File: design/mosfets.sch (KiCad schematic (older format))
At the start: 15 parts, among them Q1 Si2302CDS, Q2 Si2302CDS, Q3 Si2302CDS, Q4 Si2302CDS, Q5 Si2302CDS, Q6 Si2302CDS

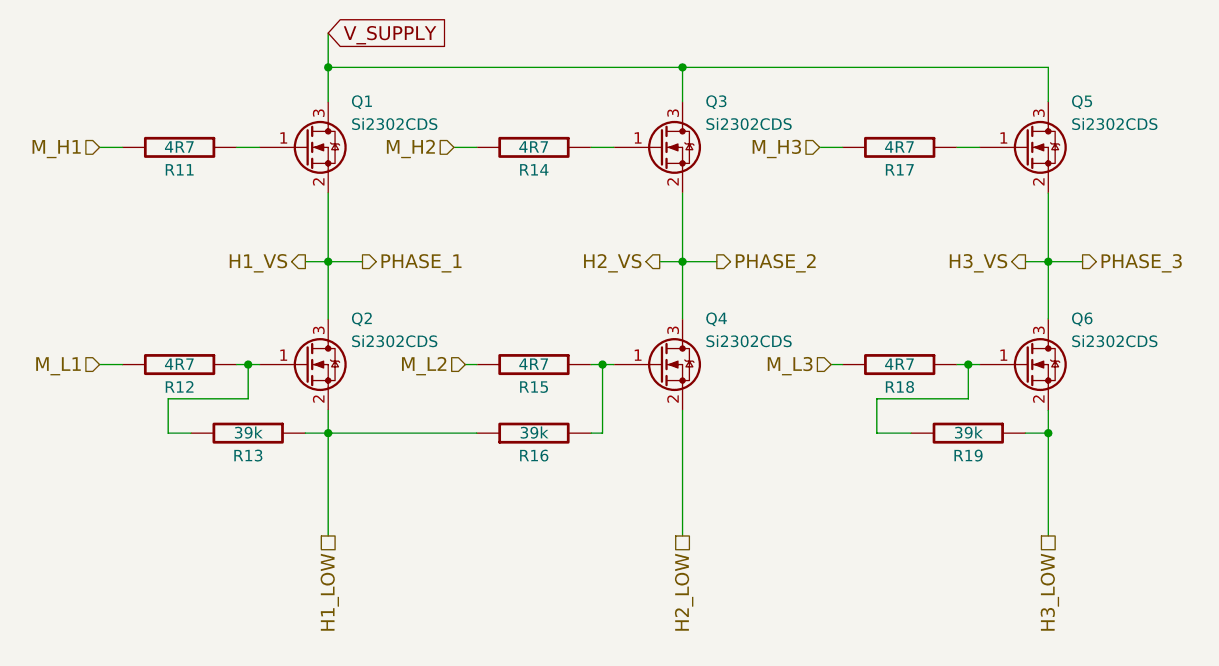
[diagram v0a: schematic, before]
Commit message: Added BOM and reworked component naming to be inline with old VESC names
:^)
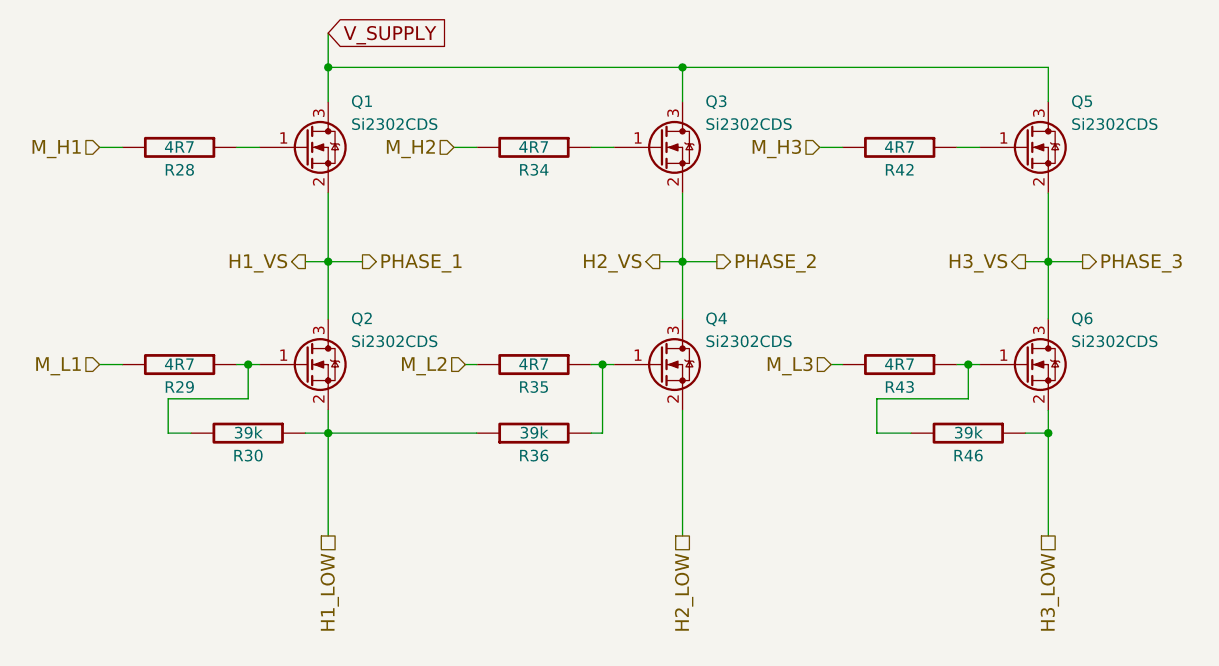
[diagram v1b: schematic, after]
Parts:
- renumbered R11 to R28, R12 to R29, R13 to R30, R14 to R34, R15 to R35, R16 to R36, R17 to R42, R18 to R43, R19 to R46
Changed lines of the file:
@@
 $EndDescr
 $Comp
-L BLDC_4-rescue:R-RESCUE-BLDC_4 R19
+L BLDC_4-rescue:R-RESCUE-BLDC_4 R46
 U 1 1 53F8E60B
 P 7850 4050
-F 0 "R19" V 7950 4050 50  0000 C CNN
+F 0 "R46" V 7950 4050 50  0000 C CNN
 F 1 "39k" V 7850 4050 50  0000 C CNN
 F 2 "Resistor_SMD:R_0603_1608Metric" H 7850 4050 60  0001 C CNN
@@
 $EndComp
 $Comp
-L BLDC_4-rescue:R-RESCUE-BLDC_4 R13
+L BLDC_4-rescue:R-RESCUE-BLDC_4 R30
 U 1 1 53F8E612
 P 4700 4050
-F 0 "R13" V 4800 4050 50  0000 C CNN
+F 0 "R30" V 4800 4050 50  0000 C CNN
 F 1 "39k" V 4700 4050 50  0000 C CNN
 F 2 "Resistor_SMD:R_0603_1608Metric" H 4700 4050 60  0001 C CNN
@@
 $EndComp
 $Comp
-L BLDC_4-rescue:R-RESCUE-BLDC_4 R12
+L BLDC_4-rescue:R-RESCUE-BLDC_4 R29
 U 1 1 53F8E64B
 P 4400 3750
-F 0 "R12" V 4500 3750 50  0000 C CNN
+F 0 "R29" V 4500 3750 50  0000 C CNN
 F 1 "4R7" V 4400 3750 50  0000 C CNN
 F 2 "Resistor_SMD:R_0603_1608Metric" H 4400 3750 60  0001 C CNN
@@
 $EndComp
 $Comp
-L BLDC_4-rescue:R-RESCUE-BLDC_4 R11
+L BLDC_4-rescue:R-RESCUE-BLDC_4 R28
 U 1 1 53F8E652
 P 4400 2800
-F 0 "R11" V 4500 2800 50  0000 C CNN
+F 0 "R28" V 4500 2800 50  0000 C CNN
 F 1 "4R7" V 4400 2800 50  0000 C CNN
 F 2 "Resistor_SMD:R_0603_1608Metric" H 4400 2800 60  0001 C CNN
@@
 $EndComp
 $Comp
-L BLDC_4-rescue:R-RESCUE-BLDC_4 R14
+L BLDC_4-rescue:R-RESCUE-BLDC_4 R34
 U 1 1 53F8E65E
 P 5950 2800
-F 0 "R14" V 6050 2800 50  0000 C CNN
+F 0 "R34" V 6050 2800 50  0000 C CNN
 F 1 "4R7" V 5950 2800 50  0000 C CNN
 F 2 "Resistor_SMD:R_0603_1608Metric" H 5950 2800 60  0001 C CNN
@@
 $EndComp
 $Comp
-L BLDC_4-rescue:R-RESCUE-BLDC_4 R15
+L BLDC_4-rescue:R-RESCUE-BLDC_4 R35
 U 1 1 53F8E665
 P 5950 3750
-F 0 "R15" V 6050 3750 50  0000 C CNN
+F 0 "R35" V 6050 3750 50  0000 C CNN
 F 1 "4R7" V 5950 3750 50  0000 C CNN
 F 2 "Resistor_SMD:R_0603_1608Metric" H 5950 3750 60  0001 C CNN
@@
 $EndComp
 $Comp
-L BLDC_4-rescue:R-RESCUE-BLDC_4 R18
+L BLDC_4-rescue:R-RESCUE-BLDC_4 R43
 U 1 1 53F8E688
 P 7550 3750
-F 0 "R18" V 7650 3750 50  0000 C CNN
+F 0 "R43" V 7650 3750 50  0000 C CNN
 F 1 "4R7" V 7550 3750 50  0000 C CNN
 F 2 "Resistor_SMD:R_0603_1608Metric" H 7550 3750 60  0001 C CNN
@@
 $EndComp
 $Comp
-L BLDC_4-rescue:R-RESCUE-BLDC_4 R17
+L BLDC_4-rescue:R-RESCUE-BLDC_4 R42
 U 1 1 53F8E68F
 P 7550 2800
-F 0 "R17" V 7650 2800 50  0000 C CNN
+F 0 "R42" V 7650 2800 50  0000 C CNN
 F 1 "4R7" V 7550 2800 50  0000 C CNN
 F 2 "Resistor_SMD:R_0603_1608Metric" H 7550 2800 60  0001 C CNN
@@
 $EndComp
 $Comp
-L BLDC_4-rescue:R-RESCUE-BLDC_4 R16
+L BLDC_4-rescue:R-RESCUE-BLDC_4 R36
 U 1 1 53F8E69C
 P 5950 4050
-F 0 "R16" V 5850 4050 50  0000 C CNN
+F 0 "R36" V 5850 4050 50  0000 C CNN
 F 1 "39k" V 5950 4050 50  0000 C CNN
 F 2 "Resistor_SMD:R_0603_1608Metric" H 5950 4050 60  0001 C CNN
